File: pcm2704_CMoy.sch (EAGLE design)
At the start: 70 parts, among them IC1 PCM2704, IC2 OPA2134P, IC4 7805TV, Q1 12MHz, X1 PG203J, X2 PN61729-S, X3 22-23-2031, X4 22-23-2031, X5 22-23-2031, X6 22-23-2031, X7 22-23-2021, X8 22-23-2021

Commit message: - Replaced current pot with Alps RK097
 - Removed old (virtual ground) power source

 - Added reverse polarity protection diode - still needs work (should it be a mosfet?)
 - Added polyfuse
 - Added +15V rail
 - Added -15V rail (TC962)
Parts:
- removed R12: PC16D, piher:PC16D
- removed U$1: TLE2426ILP, tle2426:TLE2426ILP
- removed X3, X4: 22-23-2031, con-molex:22-23-2031
- removed X7, X8: 22-23-2021, con-molex:22-23-2021
- added -15V, 15V: TPTP20R, testpad:TPTP20R
- added C13: 22uF, rcl:CPOL-EUE2.5-7
- added C21: 220uF, rcl:CPOL-EUE2.5-7
- added C22, C25: 100uF, rcl:CPOL-EUE2.5-7
- added C23, C24: 100nF, rcl:C-EUC1206
- added D1: 1N4004, diode:1N4004
- added F1: (no value), adafruit:PTCFUSE-1812
- added FREQX2: (no value), jumper:JP1E
- added IC3: 7815DT, linear:7815DT
- added IC5: 7915TV, linear:7815TV
- added MP1: (no value), sym:PMOS
- added U$2: (no value), audio-pots:ALPS_RK0971221Z0N
- added U3: TC962EPA, microchip-chargepump:TC962EPA
- C14, C15: value 0.1uF -> 100nF; device capacitor-wima:C7.5/4 -> rcl:C-EUC1206
- C18: value 470uF/25V -> 100uF; device rcl:CPOL-EUE5-10.5 -> rcl:CPOL-EUE2.5-7
- renumbered IC1 to U1, IC2 to U2, R19 to RSUPP_R, R20 to RSUPP_L
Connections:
- removed net AMP_GND: C15.2, C18.-, R12.1E, R12.2E, U$1.COM, U2A.V-, X7-2.S
- removed net AMP_VCC: C14.1, C18.+, U$1.IN, U2A.V+, X7-1.S
- new net +15V: 15V.TP, C14.2, C18.+, IC3.VO, U3.VDD
- new net +18V: CN1.PWR, D1.A, VCC.TP
- new net -15V: -15V.TP, C24.1, C25.-, IC5.VO
- new net AMP_V+: U2A.V+
- new net AMP_V-: U2A.V-
- new net N$1: D1.C, F1.1
- new net N$24: C15.2, C21.+, F1.2, IC3.VI
- new net N$30: C13.+, U3.C+
- new net N$31: C13.-, U3.C-
- new net N$33: FREQX2.1, U3.FREQX2
- new net N$34: C22.-, C23.1, IC5.VI, U3.VOUT
- net +12V: no longer CN1.PWR, VCC.TP, X8-1.S
- net AMP_OUT_LEFT: no longer X3-1.S, X4-1.S
- net AMP_OUT_RIGHT: no longer X3-3.S, X4-3.S
- net DAC_OUT_LEFT: now also U$2L.1; no longer R12.2A
- net DAC_OUT_RIGHT: now also U$2R.1; no longer R12.1A
- net GND: now also C14.1, C18.-, C21.-, C22.+, C23.2, C24.2, C25.+, FREQX2.2, IC3.GND, IC5.GND, U$2L.3, U$2R.3, U3.GND; no longer C14.2, U$1.OUT, X3-2.S, X4-2.S, X8-2.S
- net N$19: now also U$2R.2; no longer R12.1S
- net N$21: now also U$2L.2; no longer R12.2S
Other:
- note added: "NOTE: - This (RSUPP_R/RSUPP_L) should only be populated if noise supression is needed - https://tangentsoft.net/audio/cmoy/tweaks.html#r5"
- note added: "PCM2704 USB DAC"
- note removed: "12V power adapter"
- note removed: "PCM2704 USB DAC 1.1"
- note removed: "TODO: - This should only be populated if noise supression is needed - https://tangentsoft.net/audio/cmoy/tweaks.html#r5"
- note removed: "by PAVOUK"
- note removed: "http://www.isendev.com/app/entry/12"
- note removed: "http://www.pavouk.org/hw/usbdacpcm2704/en_index.html"
- moved on the sheet: C14, C15, C16, C17, C18

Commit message: Minor component placement changes
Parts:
- added C26, C27: (no value), capacitor-wima:C7.5/4
- added R12, R19: (no value), rcl:R-EU_0204/7
- added S1: (no value), switch:LPV-1
- D1: value 1N4004 -> ES2D; device diode:1N4004 -> diode:ES2D
- FREQX2: device jumper:JP1E -> jumper:SJ
- IC4: value 7805TV -> tsr 1-2433
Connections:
- removed net AMP_V+: U2A.V+
- removed net AMP_V-: U2A.V-
- new net N$33: RSUPP_R.2, U2A.OUT
- new net N$35: RSUPP_L.2, U2B.OUT
- new net N$36: C26.1, R12.2
- new net N$37: C26.2, R12.1
- net +15V: now also U2A.V+
- net -15V: now also U2A.V-
- net AMP_OUT_LEFT: now also R17.1
- net AMP_OUT_RIGHT: now also R18.1
- net N$13: now also C27.2, R19.1; no longer R17.1, RSUPP_R.2, U2A.OUT
- net N$14: now also C27.1, R19.2; no longer R18.1, RSUPP_L.2, U2B.OUT
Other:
- note added: "-15V SOURCE"
- note added: "15V SOURCE"
- note added: "TODO: - Figure out what to do whit this pin (maybe turn off the amp?)"
- note added: "TODO: - Figure out what to do whit this switch"
- note added: "TODO: - Replace pot with Alps RK097"
- note removed: "TODO: - Replace cap with Alps RK097"
- moved on the sheet: R17, R18, RSUPP_L, RSUPP_R, U2B

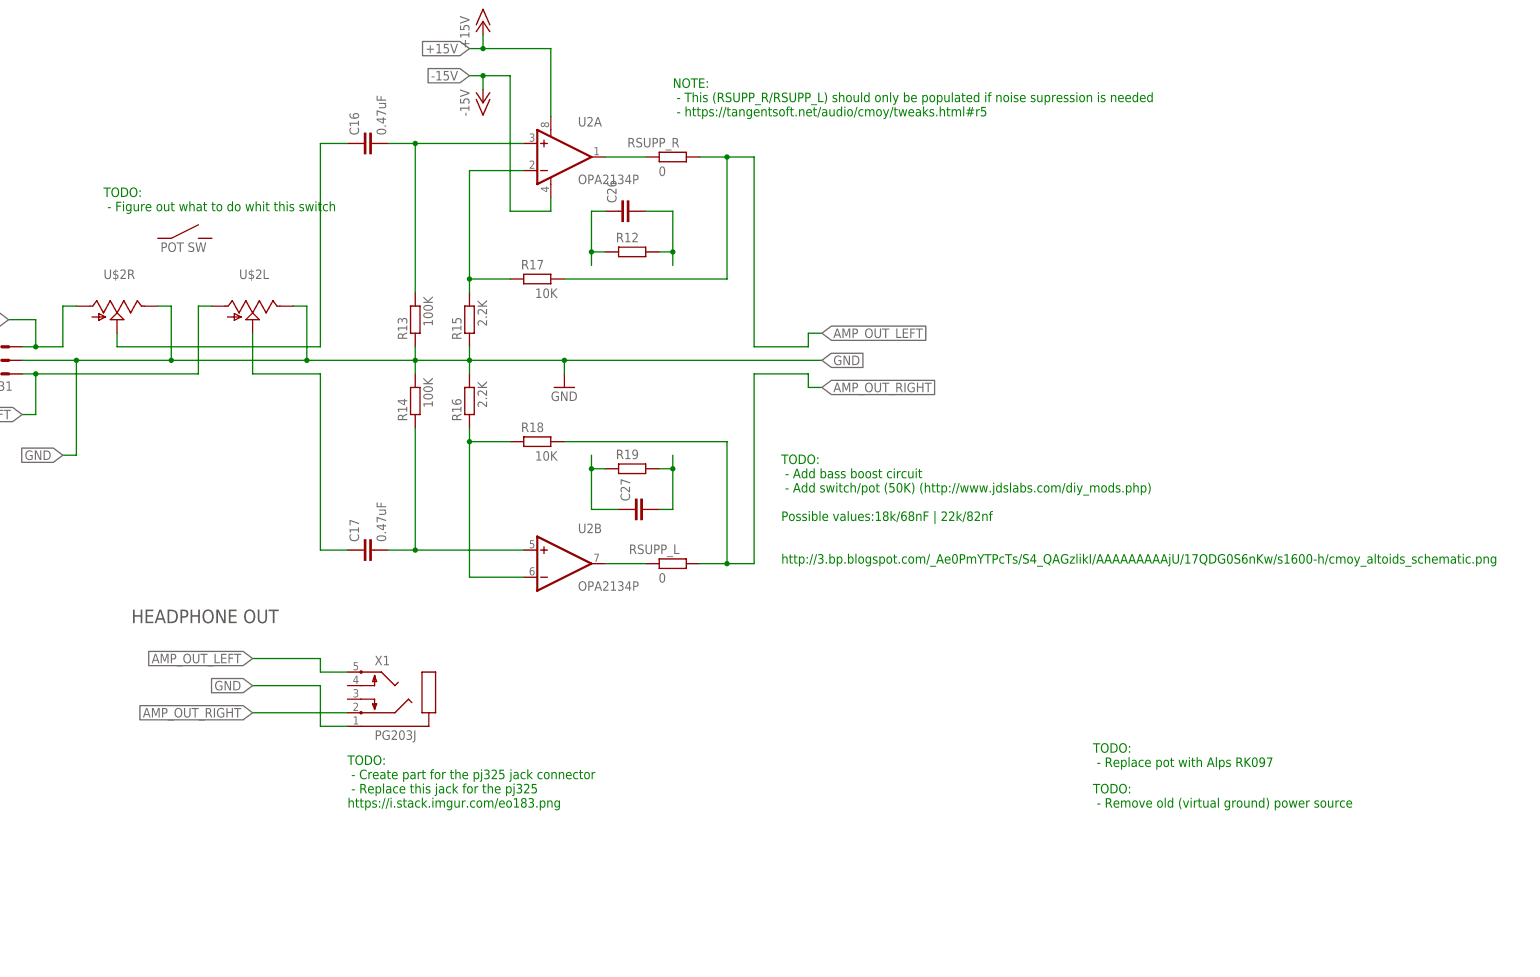
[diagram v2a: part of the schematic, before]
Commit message: - Replaced the audio jack with a PF325
 - Renamed the resistors and the capacitors in the amp to reflect the side they are used on (R/L)
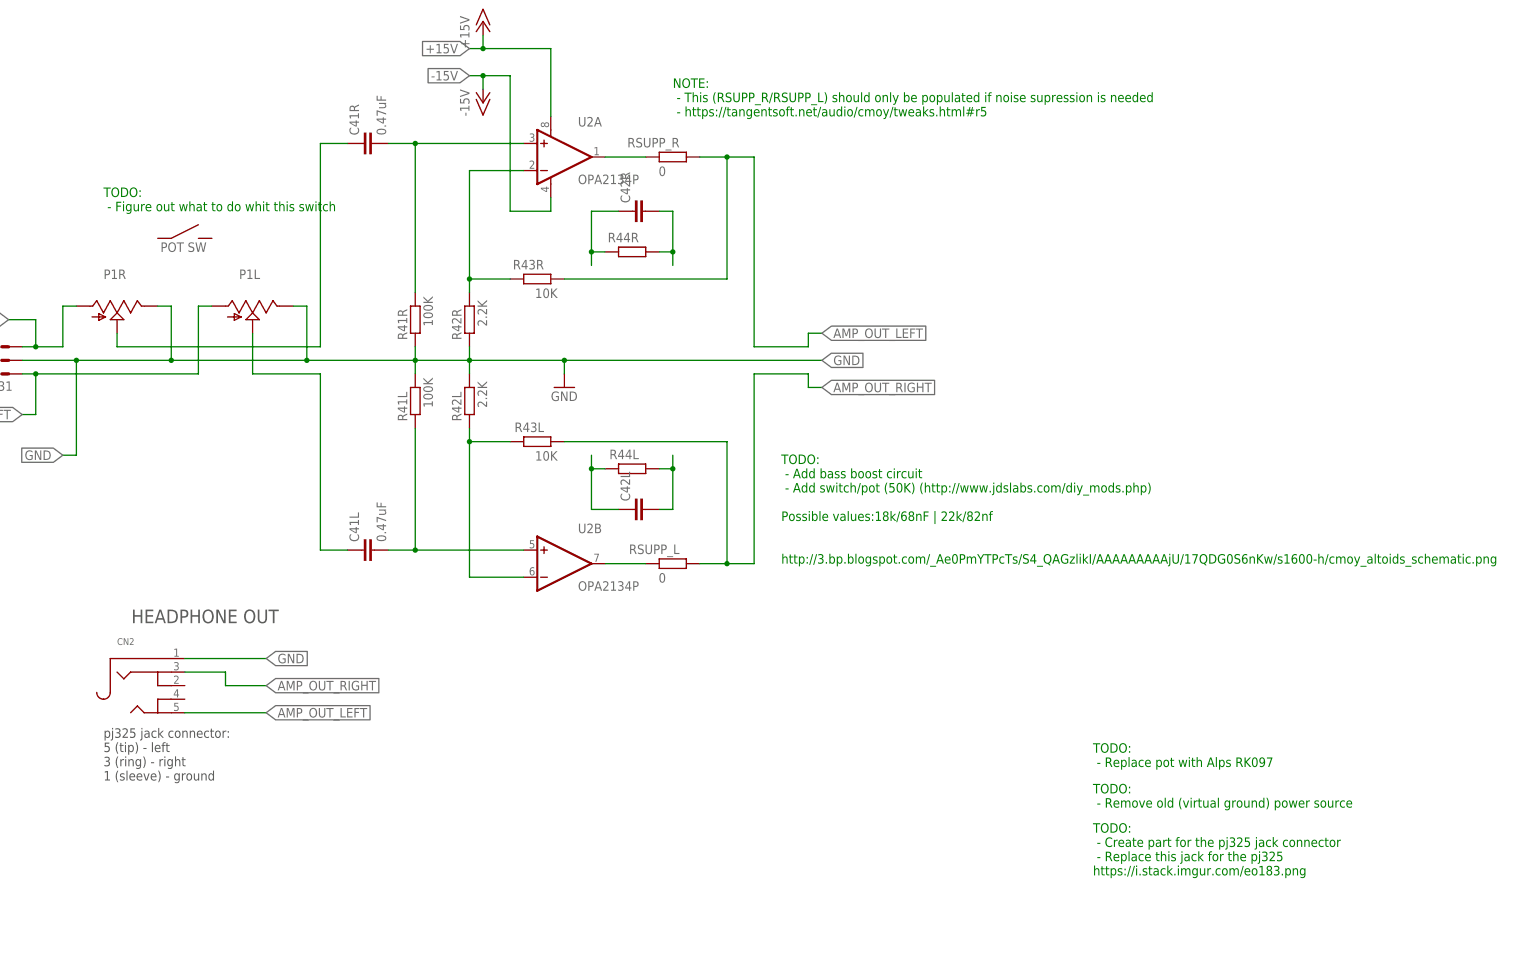
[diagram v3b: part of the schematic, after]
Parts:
- removed C26: (no value), capacitor-wima:C7.5/4
- removed X1: PG203J, con-hirschmann:PG203J
- added C42R: (no value), capacitor-wima:C7.5/4
- added CN2: (no value), microbuilder:AUDIO_3.5MMJACKPTH
- renumbered C16 to C41R, C17 to C41L, C27 to C42L, R12 to R44R, R13 to R41R, R14 to R41L, R15 to R42R, R16 to R42L, R17 to R43R, R18 to R43L, R19 to R44L, U$2 to P1
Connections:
- net AMP_OUT_LEFT: now also CN2.P$5; no longer X1.5
- net AMP_OUT_RIGHT: now also CN2.P$2; no longer X1.2
- net GND: now also CN2.P$1; no longer X1.1
- net N$36: now also C42R.1; no longer C26.1
- net N$37: now also C42R.2; no longer C26.2
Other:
- note added: "pj325 jack connector: 5 (tip) - left 3 (ring) - right 1 (sleeve) - ground"

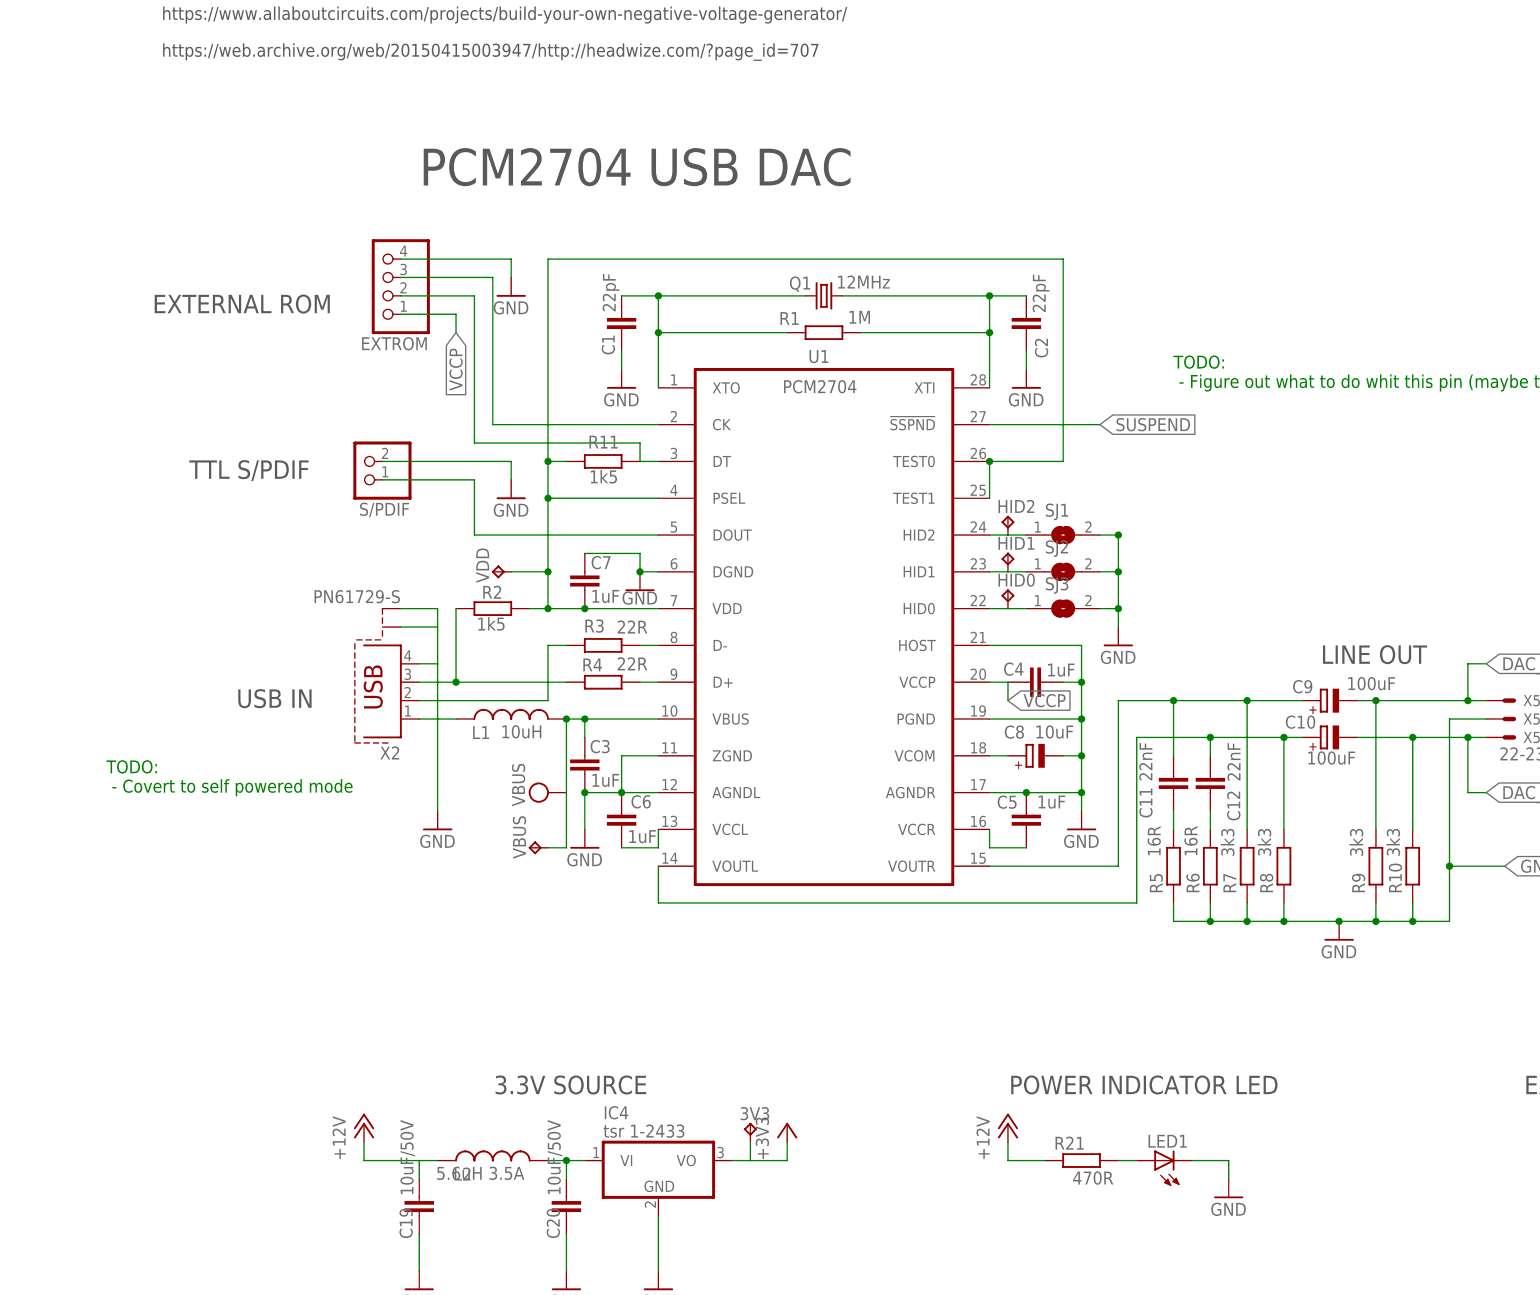
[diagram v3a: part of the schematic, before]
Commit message: - Modified PCM2704 to be self powered
 - Modified the resistor names of the dac to match the example schematic in the datasheet
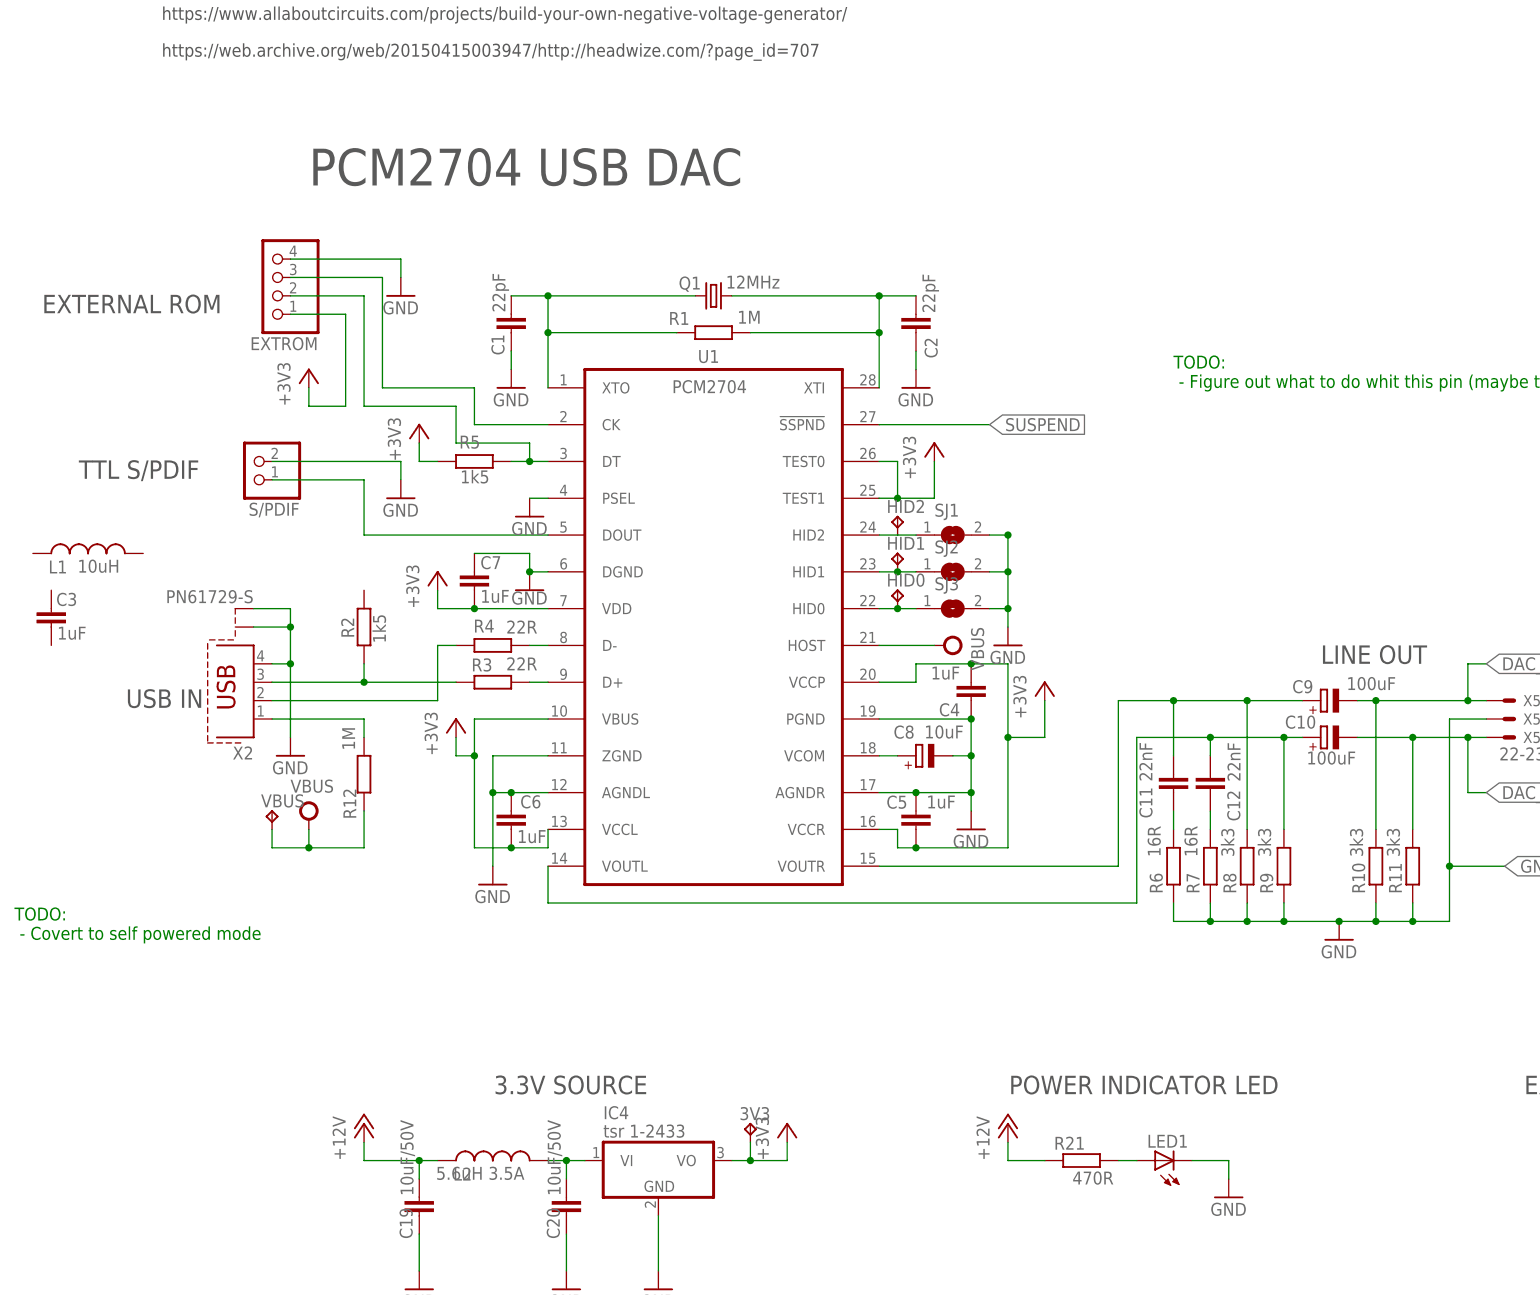
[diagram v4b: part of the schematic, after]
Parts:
- removed VDD: TPTP20R, testpad:TPTP20R
- added R12: 1M, rcl:R-EU_M0805
- R11: value 1k5 -> 3k3; device rcl:R-EU_R0805 -> rcl:R-EU_0204/7
- R5: value 16R -> 1k5; device rcl:R-EU_0204/7 -> rcl:R-EU_R0805
- R7: value 3k3 -> 16R
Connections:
- removed net VCCL: C6.2, U1.VCCL
- removed net VCCP: C4.1, EXTROM.1, U1.VCCP
- removed net VCCR: C5.1, U1.VCCR
- removed net VDD: C7.2, R11.1, R2.2, U1.PSEL, U1.TEST0, U1.TEST1, U1.VDD, VDD.TP
- net +3V3: now also C4.2, C5.1, C6.2, C7.2, EXTROM.1, R5.1, U1.TEST0, U1.TEST1, U1.VBUS, U1.VCCL, U1.VCCP, U1.VCCR, U1.VDD
- net DAC_OUT_LEFT: now also R11.2; no longer R10.2
- net DAC_OUT_RIGHT: now also R10.2; no longer R9.2
- net GND: now also C4.1, R11.1, U1.PSEL; no longer C3.2, C4.2, R5.1, U1.HOST
- net N$2: now also R12.2; no longer L1.1
- net N$20: now also R5.2; no longer R11.2
- net N$26: now also R6.2; no longer R5.2
- net N$27: now also R7.2; no longer R6.2
- net N$28: now also R8.2; no longer R7.2
- net N$29: now also R9.2; no longer R8.2
- net N$3: now also R4.1; no longer R3.1
- net N$4: now also R4.2; no longer R3.2
- net N$5: now also R3.1; no longer R4.1
- net N$6: now also R3.2; no longer R4.2
- net VBUS: now also R12.1, U1.HOST; no longer C3.1, L1.2, U1.VBUS
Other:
- moved on the sheet: C1, C2, C3, C4, C5, C6, C7, C8, EXTROM, HID0, HID1, HID2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
